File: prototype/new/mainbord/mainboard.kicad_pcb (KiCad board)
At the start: 4 copper layers, 80 x 69.3 mm, 70 parts, among them J1 SWD, J1-SCANNING1 AFC01-S16FCA-00, J10 com_adc, J17 usb_B, J2-SCANNING2 AFC01-S16FCA-00, J3 5V conn, J3-MEASURING1 AFC01-S16FCA-00, J4 GND conn, J4-MEASURING2 AFC01-S16FCA-00, J9 com_mux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

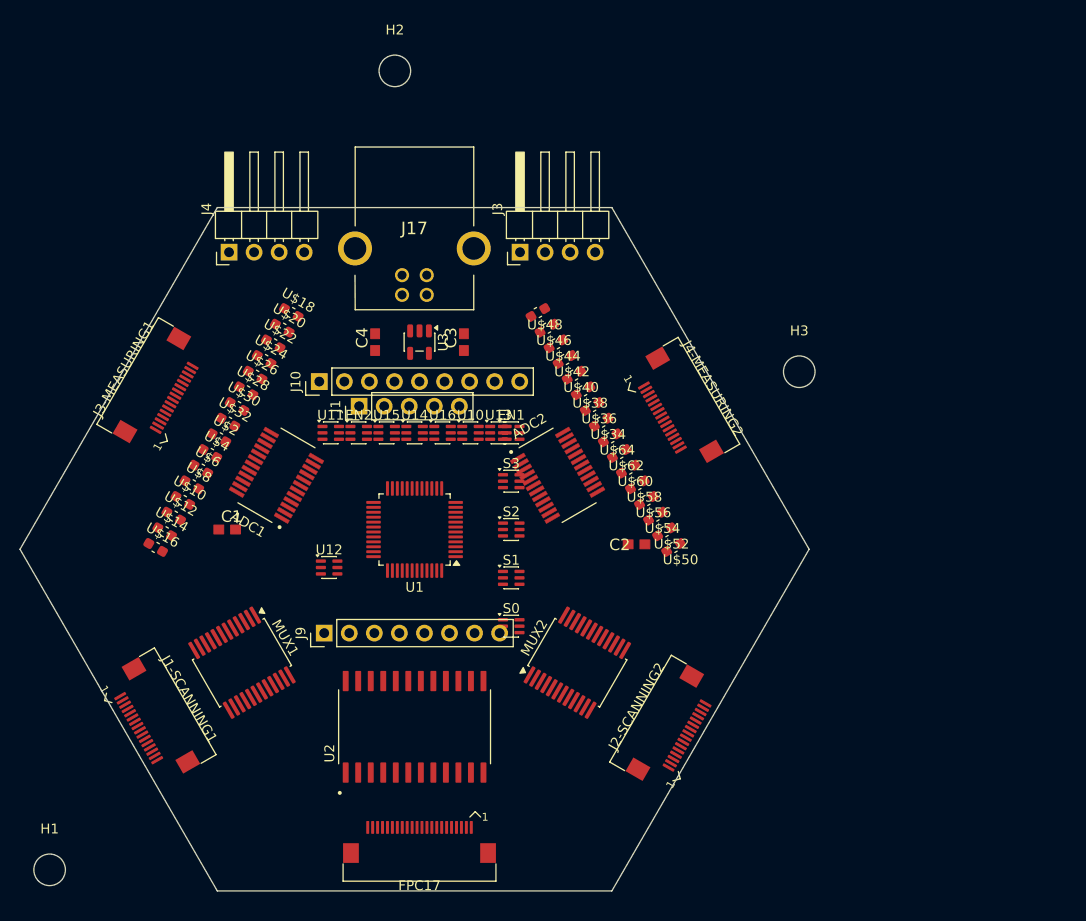
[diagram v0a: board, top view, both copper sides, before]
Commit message: Adjust mainboard PCB symmetry
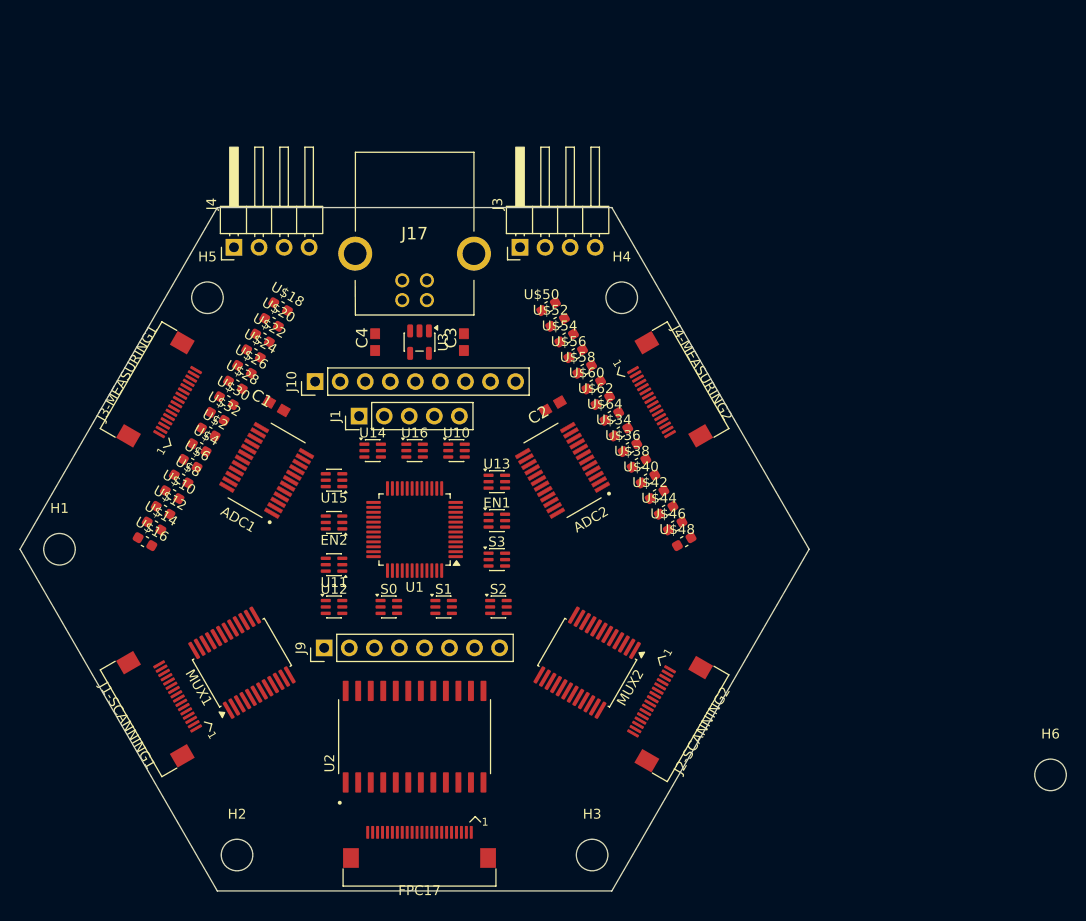
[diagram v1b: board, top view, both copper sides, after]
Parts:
- added H4: MountingHole, MountingHole:MountingHole_3.2mm_M3, F.Cu at (174.0, 70.5)
- added H5: MountingHole, MountingHole:MountingHole_3.2mm_M3, F.Cu at (132.0, 70.5)
- added H6: MountingHole, MountingHole:MountingHole_3.2mm_M3, F.Cu at (217.5, 118.9)
- moved H2 81.1 mm to (135.0, 127.0)
- moved H3 53.3 mm to (171.0, 127.0)
- moved H1 32.5 mm to (117.0, 96.0)
- moved U$48 27.6 mm to (180.3, 95.2), turned to 30 degrees
- moved U$50 27.5 mm to (166.6, 71.4), turned to 30 degrees
- moved U$46 23.9 mm to (179.4, 93.6), turned to 30 degrees
- moved U$52 23.8 mm to (167.5, 73.0), turned to 30 degrees
- moved U$44 20.2 mm to (178.5, 92.1), turned to 30 degrees
- moved U$54 20.2 mm to (168.4, 74.6), turned to 30 degrees
- moved U$42 16.6 mm to (177.6, 90.5), turned to 30 degrees
- moved U$56 16.5 mm to (169.3, 76.2), turned to 30 degrees
- moved C2 16.4 mm to (167.0, 81.5), turned to 30 degrees
- moved C1 13.5 mm to (139.0, 81.5), turned to -30 degrees
- moved U11 13.4 mm to (144.8, 97.6), turned to 180 degrees
- moved U$40 12.9 mm to (176.7, 88.9), turned to 30 degrees
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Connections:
- S2 pad 3: /S3' -> /S2'

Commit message: Sync current mainboard hardware
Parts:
- moved H6 36.5 mm to (189.0, 96.0)
- moved U$50 28.1 mm to (168.0, 99.5), turned to 180 degrees
- moved U$48 26.3 mm to (168.0, 72.0), turned to 180 degrees
- moved U$52 24.7 mm to (168.0, 97.7), turned to 180 degrees
- moved U$46 22.9 mm to (168.0, 73.8), turned to 180 degrees
- moved U$54 21.2 mm to (168.0, 95.8), turned to 180 degrees
- moved U$44 19.5 mm to (168.0, 75.7), turned to 180 degrees
- moved C1 18.1 mm to (122.5, 89.0), turned to 90 degrees
- moved C2 18.1 mm to (183.5, 89.0), turned to 90 degrees
- moved U$56 17.9 mm to (168.0, 94.0), turned to 180 degrees
- moved U$42 16.1 mm to (168.0, 77.5), turned to 180 degrees
- moved U$58 14.6 mm to (168.0, 92.2), turned to 180 degrees
- moved U$16 13.5 mm to (138.5, 99.5), turned to 0 degrees
- moved U$40 12.9 mm to (168.0, 79.3), turned to 180 degrees
- moved U$14 12.6 mm to (138.5, 97.7), turned to 0 degrees
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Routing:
- net +3.3V: track 0.00 -> 129.2 mm, vias 0 -> 13
- net GND: track 0.00 -> 121.3 mm, vias 0 -> 46
- net +5V: track 0.00 -> 100.6 mm, vias 0 -> 16
- added copper zone on In2.Cu, net +3.3V
- added copper zone on In2.Cu, net +5V
- added copper zone on In1.Cu, net GND
